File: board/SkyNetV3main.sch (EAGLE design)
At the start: 37 parts, among them IC1 LPC1768, Q1 12MHz, Q2 32.768KHz, U1 HC_05

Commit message: further schematics development; layout started
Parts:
- removed RADIO: RF4463PRO, RF4436PRO:RF4463PRO
- removed U$2: BCX17, skynet_other:BCX17
- removed U$3: UCC3954, UCC3954:UCC3954
- removed U1: HC_05, Bluetooth HC-05:HC_05
- removed USB2: MOLEX-47346-0001, usb_con-update:MOLEX-47346-0001
- added C10: 4u7, rcl:C-EUC1206K
- added C11: 100n, rcl:C-EUC1206K
- added C12, C13, C14, C18, C19, C20, C21: 100n, rcl:C-EUC0603
- added C22, C23: 18p, rcl:C-EUC0603
- added C6: 10u, rcl:C-EUC1206K
- added IC2: RF4463PRO, RF4436PRO:RF4463PRO
- added IC3: LPC1768, lpc1xxx-v6:LPC1768
- added IC4: BCX17, skynet_other:BCX17
- added IC5: TPS63001, texas:TPS6300
- added IC6: MCP73871-2CCI/ML, microchip-battery:MCP73871-2CCI/ML
- added JP3: JTAG, microbuilder:HEADER-2X51.27MM
- added JP4: PERIPH, microbuilder:HEADER-2X51.27MM
- added L1: 2u2, skynet_other:LPS4012
- added OK1, OK2, OK3: PC3H7, skynet_other:PC3H7
- added Q3: IRLM6402, microbuilder:MOSFET-PWIDE
- added Q4: BSS138, microbuilder:MOSFET-NWIDE
- added R11, R12: 10k, rcl:R-EU_R0603
- added R15, R16: 33, rcl:R-EU_R0603
- added R17: 100, rcl:R-EU_R0603
- added R18, R19: 68, rcl:R-EU_R0603
- added S3: INPUT, skynet_other:PT645VERT
- added USB1: MOLEX-47346-0001, usb_con-update:MOLEX-47346-0001
- added X1: BAT, con-molex:22-23-2021
- C1: device capacitor-wima:C2.5/2 -> rcl:C-EUC1206K
- C15: value 100u -> 100n; device rcl:CPOL-EU153CLV-1010 -> rcl:C-EUC0603
- C16, C17: value 18p -> 100n; device capacitor-wima:C2.5/2 -> rcl:C-EUC0603
- C2, C3: value 5p -> 18p; device capacitor-wima:C2.5/2 -> rcl:C-EUC0603
- C4, C5: value 18p -> 33p; device capacitor-wima:C2.5/2 -> rcl:C-EUC0603
- C7, C8: device rcl:C-EUC1206 -> rcl:C-EUC1206K
- C9: value 10u -> 4u7; device rcl:C-EUC1206 -> rcl:C-EUC1206K
- IC1: value LPC1768 -> HC_05; device lpc1xxx-v6:LPC1768 -> Bluetooth HC-05:HC_05
- JP1: value PROG -> MEASURE
- JP2: value ANT -> DEBUG; device pinhead:PINHD-1X2 -> pinhead:PINHD-1X5
- LED1: value OVSTRGBBCR8 -> STATUS; device led:OVSTRGBBCR8 -> skynet_other:RGB-LED
- Q1: value 12MHz -> 32.768KHz; device special:XTAL -> crystal-2:CRYSTALMM20SS
- Q2: value 32.768KHz -> 12MHz; device special:XTAL -> microbuilder:CRYSTALSMD
- R1: value 38,3 -> 10k; device resistor:R-EU_R1206 -> rcl:R-EU_R0603
- R10: value 1k5 -> 560; device resistor:R-EU_R1206 -> rcl:R-EU_R0603
- R13: value 33 -> 10k; device resistor:R-EU_R1206 -> rcl:R-EU_R0603
- R14: value 33 -> 100k; device resistor:R-EU_R1206 -> rcl:R-EU_R0603
- R2: value 24,9 -> 10K; device resistor:R-EU_R1206 -> rcl:R-EU_R0603
- R3: value 38,3 -> 50; device resistor:R-EU_R1206 -> rcl:R-EU_R0603
- R4: value 10K -> 1k5; device resistor:R-EU_R1206 -> rcl:R-EU_R0603
- R5: device resistor:R-EU_R1206 -> rcl:R-EU_R0603
- R6, R8: value 10k -> 91; device rcl:R-EU_R1206 -> rcl:R-EU_R0603
- R7: value 1k -> 91; device rcl:R-EU_R1206 -> rcl:R-EU_R0603
- R9: value 50 -> 10k; device resistor:R-EU_R1206 -> rcl:R-EU_R0603
- S1: value INPUT -> PROG; device switch-omron:10-XX -> switch-ck:PTS645SSMTR
- S2: device switch-omron:10-XX -> switch-ck:PTS645SSMTR
- U$1: value MCP73871-1AAI/ML -> ANT-MML; device microchip-battery:MCP73871-1AAI/ML -> skynet_other:ANT-MML
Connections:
- removed net N$1: IC1.P0[21]/RI1/RD1, RADIO.SDN
- removed net N$10: IC1.P0[0]/RD1/TXD3/SDA1, U1.RX
- removed net N$11: IC1.P0[16]/RXD1/SSEL0/SSEL, RADIO.NSEL
- removed net N$12: IC1.P0[20]/DTR1/SCL1, RADIO.GPIO0
- removed net N$13: IC1.P2[2]/PWM1[3]/CTS1/TRACEDATA[3], R1.1
- removed net N$14: LED1-G.A, R3.2
- removed net N$15: IC1.P2[9]/USB_CONNECT/RXD2/ENET_MDIO, R9.1
- removed net N$16: IC1.P0[18]/DCD1/MOSI0/MOSI, RADIO.SDI
- removed net N$17: IC1.P0[17]/CTS1/MISO0/MISO, RADIO.SDO
- removed net N$18: IC1.P0[15]/TXD1/SCK0/SCK, RADIO.SCLK
- removed net N$2: IC1.P2[10]/EINT0/NMI, JP1.1, R5.1
- removed net N$20: IC1.P0[19]/DSR1/SDA1, RADIO.NIRQ
- removed net N$21: JP2.1, RADIO.ANT
- removed net N$22: R9.2, U$2.B
- removed net N$23: LED1-R.A, R2.2
- removed net N$24: R8.1, U$1.PROG3
- removed net N$25: R7.1, U$1.PROG1
- removed net N$26: R6.1, U$1.THERM
- removed net N$27: LED1G$1.A, R1.2
- removed net N$28: IC1.P2[12]/EINT2/I2STX_WS, S1.P, S1.P1
- removed net N$3: IC1.P2[0]/PWM1[1]/TXD1, R2.1
- removed net N$4: IC1.P2[1]/PWM1[2]/RXD1, R3.1
- removed net N$40: R10.2, U$2.C
- removed net N$44: C15.-, U$3.BAT-
- removed net N$49: R13.2, USB2.2
- removed net N$50: R14.2, USB2.3
- removed net N$9: IC1.P0[1]/TD1/RXD3/SCL1, U1.TX
- new net AD-IN: C15.1, IC3.P0[23]/AD0[0]/I2SRX_CLK/CAP3[0], R12.2, R13.1
- new net AD-PWR: IC3.P0[22]/RTS1/TD1, Q4.G
- new net AD-PWR-FET: Q3.G, Q4.D, R14.2
- new net AD-PWR-FET2: Q3.D, R12.1
- new net ANT: IC2.ANT, U$1.ANT
- new net BT_RX: IC1.RX, IC3.P0[0]/RD1/TXD3/SDA1
- new net BT_TX: IC1.TX, IC3.P0[1]/TD1/RXD3/SCL1
- new net CHGSEL_H: IC3.P1[0]/ENET_TXD0, IC6.SEL
- new net CHGSEL_L: IC3.P1[1]/ENET_TXD1, IC6.PROG2
- new net CHG_S1: IC3.P1[4]/ENET_TX_EN, OK3.COL
- new net CHG_S2: IC3.P1[8]/ENET_CRS, OK2.COL
- new net EXT_GPIO0: IC3.P2[3]/PWM1[4]/DCD1/TRACEDATA[2], JP4.6
- new net EXT_GPIO1: IC3.P2[4]/PWM1[5]/DSR1/TRACEDATA[1], JP4.8
- new net EXT_PWR: IC3.P2[12]/EINT2/I2STX_WS, OK1.COL
- new net INPUT: IC3.P2[11]/EINT1/I2STX_CLK, S3.P
- new net JTAG-TRST: IC3.TRST, R1.1
- new net JTAG_TCK: IC3.TCK/SWDCLK, JP3.4
- new net JTAG_TDI: IC3.TDI, JP3.8
- new net JTAG_TDO: IC3.TDO/SWO, JP3.6
- new net JTAG_TMS: IC3.TMS/SWDIO, JP3.2
- new net L1: IC5G$1.L1, L1.P1
- new net L2: IC5G$1.L2, L1.P2
- new net LED-B-R: LED1-B.A, R19.1
- new net LED-G-R: LED1-G.A, R18.1
- new net LED-R-R: LED1-R.A, R17.1
- new net LED_B: IC3.P2[2]/PWM1[3]/CTS1/TRACEDATA[3], LED1-B.C
- new net LED_G: IC3.P2[1]/PWM1[2]/RXD1, LED1-G.C
- new net LED_R: IC3.P2[0]/PWM1[1]/TXD1, LED1-R.C
- new net OUT2: C10.1, IC6.OUT, IC6.OUT2, JP1.1
- new net PG: IC6./PG, R6.1
- new net PG-OK: OK1.C, R6.2
- new net PROG: IC3.P2[10]/EINT0/NMI, R5.1, S1.P
- new net PROG1: IC6.PROG1, R10.1
- new net PROG3: IC6.PROG3, R9.1
- new net RF-GPIO0: IC2.GPIO0, IC3.P0[20]/DTR1/SCL1
- new net RX: IC3.P0[3]/RXD0/AD0[6], JP2.1
- new net SCL_EXT: IC3.P0[11]/RXD2/SCL2/MAT3[1], JP4.4
- new net SDA_EXT: IC3.P0[10]/TXD2/SDA2/MAT3[0], JP4.2
- new net SDI: IC2.SDI, IC3.P0[18]/DCD1/MOSI0/MOSI
- new net SPI0-NIRQ: IC2.NIRQ, IC3.P0[19]/DSR1/SDA1
- new net SPI0-NSEL: IC2.NSEL, IC3.P0[16]/RXD1/SSEL0/SSEL
- new net SPI0-SCLK: IC2.SCLK, IC3.P0[15]/TXD1/SCK0/SCK
- new net SPI0-SDN: IC2.SDN, IC3.P0[21]/RI1/RD1
- new net SPI0-SDO: IC2.SDO, IC3.P0[17]/CTS1/MISO0/MISO
- new net SPI2_MISO: IC3.P0[8]/I2STX_WS/MISO1/MAT2[2], JP4.5
- new net SPI2_MOSI: IC3.P0[9]/I2STX_SDA/MOSI1/MAT2[3], JP4.7
- new net SPI2_SCK: IC3.P0[7]/I2STX_CLK/SCK1/MAT2[1], JP4.3
- new net SPI2_SEL: IC3.P0[6]/I2SRX_SDA/SSEL1/MAT2[0], JP4.1
- new net STAT1: IC6.STAT1/LBO, R8.1
- new net STAT1-OK: OK3.C, R8.2
- new net STAT2: IC6.STAT2, R7.1
- new net STAT2-OK: OK2.C, R7.2
- new net THERM: IC6.THERM, R11.1
- new net TX: IC3.P0[2]/TXD0/AD0[7], JP2.3
- new net USB-CON: IC3.P2[9]/USB_CONNECT/RXD2/ENET_MDIO, R3.1
- new net USB-CON-TRANS: IC4.B, R3.2
- new net USB-CON-TRANS-2: IC4.C, R4.2
- new net USB-D+_IN: R15.2, USB1.2
- new net USB-D-_IN: R16.2, USB1.3
- net +3V3: now also C11.1, C12.1, C13.1, C14.1, C16.1, C17.1, C18.1, C19.1, C20.1, C21.1, C8.1, IC1.3V3, IC2.VCC, IC3.VBAT, IC3.VDD(3V3)1, IC3.VDD(3V3)2, IC3.VDD(3V3)3, IC3.VDD(3V3)4, IC3.VDD(REG)(3V3)1, IC3.VDD(REG)(3V3)2, IC3.VDDA, IC3.VREFP, IC4.E, IC5G$1.FB, IC5G$1.VOUT, JP2.4, JP3.1, JP4.10, R1.2, R17.2, R18.2, R19.2, R2.2; no longer R4.2, RADIO.VCC, U$2.E, U1.3V3
- net +5V: now also C6.1, IC6./TE, IC6.CE, IC6.IN, IC6.IN2, IC6.VPCC, OK1.A, OK2.A, OK3.A, USB1.1; no longer C7.1, U$1./TE, U$1.CE, U$1.IN, U$1.IN2, U$1.PROG2, U$1.SEL, U$1.VPCC, USB2.1
- net BT_AT: now also IC1.PIO11, IC3.P0[4]/I2SRX_CLK/RD2/CAP2[0]; no longer IC1.P0[4]/I2SRX_CLK/RD2/CAP2[0], U1.PIO11
- net BT_RESET: now also IC1.RST, IC3.P0[5]/I2SRX_WS/TD2/CAP2[1]; no longer IC1.P0[5]/I2SRX_WS/TD2/CAP2[1], U1.RST
- net GND: now also C10.2, C11.2, C12.2, C13.2, C14.2, C15.2, C18.2, C19.2, C20.2, C21.2, C22.2, C23.2, C6.2, IC1.GND, IC2.GND@1, IC2.GND@2, IC2.GND@3, IC3.VREFN, IC3.VSS1, IC3.VSS2, IC3.VSS3, IC3.VSS4, IC3.VSS5, IC3.VSS6, IC3.VSSA, IC5G$1.GND, IC5G$1.PGND, IC6.EP, IC6.VSS, IC6.VSS2, JP2.5, JP3.3, JP3.5, JP3.9, JP4.9, OK1.EMI, OK2.EMI, OK3.EMI, Q4.S, R10.2, R11.2, R13.2, R9.2, S2.P, S3.S, U$1.GND, USB1.5, USB1.GND1, USB1.GND2, USB1.GND3, USB1.GND4, X1-1.S; no longer C15.+, IC1.VREFN, IC1.VSS1, IC1.VSS2, IC1.VSS3, IC1.VSS4, IC1.VSS5, IC1.VSS6, IC1.VSSA, JP1.2, JP2.2, LED1-G.C, LED1-R.C, LED1G$1.C, R6.2, R7.2, R8.2, RADIO.GND$1, RADIO.GND$2, RADIO.GND$3, S1.S1, S2.S, S2.S1, U$1.EP, U$1.VSS, U$1.VSS2, U1.GND, USB2.5
- net RESET: now also IC3.RESET, JP3.10, R2.1, S2.S; no longer IC1.RESET, R4.1, S2.P, S2.P1
- net RTCX1: now also IC3.RTCX1, Q1.2; no longer IC1.RTCX1, Q2.2
- net RTCX2: now also IC3.RTCX2, Q1.1; no longer IC1.RTCX2, Q2.1
- net USB-D+: now also C22.1, IC3.P0[29]/USB_DPLUS, R15.1, R4.1; no longer C16.1, IC1.P0[29]/USB_DPLUS, R10.1, R13.1
- net USB-D-: now also C23.1, IC3.P0[30]/USB_DMINUS, R16.1; no longer C17.1, IC1.P0[30]/USB_DMINUS, R14.1
- net V+: now also C9.1, IC6.VBAT, IC6.VBAT2, IC6.VBAT_SENSE, Q3.S, R14.1, X1-2.S; no longer C8.1, U$1.VBAT, U$1.VBAT2, U$1.VBAT_SENSE
- net VCC: now also C7.1, IC5G$1.EN, IC5G$1.PS/SYNC, IC5G$1.VIN, IC5G$1.VINA, JP1.2; no longer C9.1, IC1.VBAT, IC1.VDD(3V3)1, IC1.VDD(3V3)2, IC1.VDD(3V3)3, IC1.VDD(3V3)4, IC1.VDD(REG)(3V3)1, IC1.VDD(REG)(3V3)2, IC1.VDDA, IC1.VREFP, U$1.OUT, U$1.OUT2
- net XTAL1: now also IC3.XTAL1, Q2.2; no longer IC1.XTAL1, Q1.2
- net XTAL2: now also IC3.XTAL2, Q2.1; no longer IC1.XTAL2, Q1.1
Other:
- note removed: "TODO: ISP-Header"
- note removed: "TODO: wie erkennen ob USB-Flashen?"

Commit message: further layout, got stuck somewhere...
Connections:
- removed net BT_RESET: IC1.RST, IC3.P0[5]/I2SRX_WS/TD2/CAP2[1]
- new net BT-RST: IC1.RST, IC3.P0[22]/RTS1/TD1
- net AD-PWR: now also IC3.P1[29]/MCOB2/PCAP1[1]/MAT0[1]; no longer IC3.P0[22]/RTS1/TD1
- net BT_AT: now also IC3.P2[5]/PWM1[6]/DTR1/TRACEDATA[0]; no longer IC3.P0[4]/I2SRX_CLK/RD2/CAP2[0]
- net CHGSEL_H: now also IC3.P3[25]/MAT0[0]/PWM1[2]; no longer IC3.P1[0]/ENET_TXD0
- net CHGSEL_L: now also IC3.P3[26]/STCLK/MAT0[1]/PWM1[3]; no longer IC3.P1[1]/ENET_TXD1
- net CHG_S1: now also IC3.P0[10]/TXD2/SDA2/MAT3[0]; no longer IC3.P1[4]/ENET_TX_EN
- net CHG_S2: now also IC3.P0[11]/RXD2/SCL2/MAT3[1]; no longer IC3.P1[8]/ENET_CRS
- net SCL_EXT: now also IC3.P0[28]/SCL0/USB_SCL; no longer IC3.P0[11]/RXD2/SCL2/MAT3[1]
- net SDA_EXT: now also IC3.P0[27]/SDA0/USB_SDA; no longer IC3.P0[10]/TXD2/SDA2/MAT3[0]
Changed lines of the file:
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@@
 <net name="BT_AT" class="0">
+<segment>
+<pinref part="IC3" gate="G$1" pin="P2[5]/PWM1[6]/DTR1/TRACEDATA[0]"/>
+<wire x1="185.42" y1="88.9" x2="187.96" y2="88.9" width="0.1524" layer="91"/>
+<label x="188.214" y="87.884" size="1.778" layer="95"/>
+</segment>
 <segment>
 <pinref part="IC1" gate="G$1" pin="PIO11"/>
 <wire x1="10.16" y1="162.56" x2="7.62" y2="162.56" width="0.1524" layer="91"/>
-<wire x1="7.62" y1="162.56" x2="7.62" y2="172.72" width="0.1524" layer="91"/>
-<wire x1="7.62" y1="172.72" x2="73.66" y2="172.72" width="0.1524" layer="91"/>
-<wire x1="73.66" y1="172.72" x2="73.66" y2="154.94" width="0.1524" layer="91"/>
-<pinref part="IC3" gate="G$1" pin="P0[4]/I2SRX_CLK/RD2/CAP2[0]"/>
-<wire x1="73.66" y1="154.94" x2="96.52" y2="154.94" width="0.1524" layer="91"/>
+<label x="4.572" y="168.402" size="1.778" layer="95"/>
+<wire x1="7.62" y1="162.56" x2="7.62" y2="167.64" width="0.1524" layer="91"/>
 </segment>
 </net>
@@
 </segment>
 </net>
-<net name="BT_RESET" class="0">
-<segment>
-<pinref part="IC1" gate="G$1" pin="RST"/>
-<wire x1="58.42" y1="137.16" x2="60.96" y2="137.16" width="0.1524" layer="91"/>
-<wire x1="60.96" y1="137.16" x2="60.96" y2="152.4" width="0.1524" layer="91"/>
-<pinref part="IC3" gate="G$1" pin="P0[5]/I2SRX_WS/TD2/CAP2[1]"/>
-<wire x1="60.96" y1="152.4" x2="96.52" y2="152.4" width="0.1524" layer="91"/>
-</segment>
-</net>
 <net name="RF-GPIO0" class="0">
 <segment>
@@
 <net name="CHGSEL_H" class="0">
 <segment>
-<pinref part="IC3" gate="G$1" pin="P1[0]/ENET_TXD0"/>
-<wire x1="185.42" y1="165.1" x2="193.04" y2="165.1" width="0.1524" layer="91"/>
-<label x="193.802" y="164.338" size="1.778" layer="95"/>
+<pinref part="IC3" gate="G$1" pin="P3[25]/MAT0[0]/PWM1[2]"/>
+<wire x1="185.42" y1="63.5" x2="187.96" y2="63.5" width="0.1524" layer="91"/>
+<wire x1="187.96" y1="63.5" x2="187.96" y2="68.58" width="0.1524" layer="91"/>
+<wire x1="187.96" y1="68.58" x2="193.04" y2="68.58" width="0.1524" layer="91"/>
+<label x="193.294" y="67.564" size="1.778" layer="95"/>
 </segment>
 </net>
 <net name="CHGSEL_L" class="0">
 <segment>
-<pinref part="IC3" gate="G$1" pin="P1[1]/ENET_TXD1"/>
-<wire x1="185.42" y1="162.56" x2="193.04" y2="162.56" width="0.1524" layer="91"/>
-<label x="193.802" y="161.798" size="1.778" layer="95"/>
+<pinref part="IC3" gate="G$1" pin="P3[26]/STCLK/MAT0[1]/PWM1[3]"/>
+<wire x1="185.42" y1="60.96" x2="190.5" y2="60.96" width="0.1524" layer="91"/>
+<wire x1="190.5" y1="60.96" x2="190.5" y2="66.04" width="0.1524" layer="91"/>
+<wire x1="190.5" y1="66.04" x2="193.04" y2="66.04" width="0.1524" layer="91"/>
+<label x="193.294" y="65.024" size="1.778" layer="95"/>
 </segment>
 </net>
@@
 <net name="CHG_S1" class="0">
 <segment>
-<pinref part="IC3" gate="G$1" pin="P1[4]/ENET_TX_EN"/>
-<wire x1="185.42" y1="160.02" x2="193.04" y2="160.02" width="0.1524" layer="91"/>
-<label x="193.802" y="159.258" size="1.778" layer="95"/>
+<pinref part="IC3" gate="G$1" pin="P0[10]/TXD2/SDA2/MAT3[0]"/>
+<wire x1="96.52" y1="139.7" x2="93.98" y2="139.7" width="0.1524" layer="91"/>
+<label x="92.964" y="139.192" size="1.778" layer="95" rot="MR0"/>
 </segment>
 </net>
 <net name="CHG_S2" class="0">
 <segment>
-<pinref part="IC3" gate="G$1" pin="P1[8]/ENET_CRS"/>
-<wire x1="185.42" y1="157.48" x2="193.04" y2="157.48" width="0.1524" layer="91"/>
-<label x="193.802" y="156.718" size="1.778" layer="95"/>
+<pinref part="IC3" gate="G$1" pin="P0[11]/RXD2/SCL2/MAT3[1]"/>
+<wire x1="96.52" y1="137.16" x2="93.98" y2="137.16" width="0.1524" layer="91"/>
+<label x="92.964" y="136.652" size="1.778" layer="95" rot="MR0"/>
 </segment>
 </net>
@@
 <net name="SDA_EXT" class="0">
 <segment>
-<pinref part="IC3" gate="G$1" pin="P0[10]/TXD2/SDA2/MAT3[0]"/>
-<wire x1="96.52" y1="139.7" x2="93.98" y2="139.7" width="0.1524" layer="91"/>
-<label x="92.964" y="139.192" size="1.778" layer="95" rot="MR0"/>
+<pinref part="IC3" gate="G$1" pin="P0[27]/SDA0/USB_SDA"/>
+<wire x1="96.52" y1="104.14" x2="93.98" y2="104.14" width="0.1524" layer="91"/>
+<label x="93.472" y="103.378" size="1.778" layer="95" rot="MR0"/>
 </segment>
 </net>
 <net name="SCL_EXT" class="0">
 <segment>
-<pinref part="IC3" gate="G$1" pin="P0[11]/RXD2/SCL2/MAT3[1]"/>
-<wire x1="96.52" y1="137.16" x2="93.98" y2="137.16" width="0.1524" layer="91"/>
-<label x="92.964" y="136.652" size="1.778" layer="95" rot="MR0"/>
+<pinref part="IC3" gate="G$1" pin="P0[28]/SCL0/USB_SCL"/>
+<wire x1="96.52" y1="101.6" x2="93.98" y2="101.6" width="0.1524" layer="91"/>
+<label x="93.472" y="100.838" size="1.778" layer="95" rot="MR0"/>
 </segment>
 </net>
 <net name="AD-PWR" class="0">
+<segment>
+<pinref part="IC3" gate="G$1" pin="P1[29]/MCOB2/PCAP1[1]/MAT0[1]"/>
+<wire x1="185.42" y1="111.76" x2="187.96" y2="111.76" width="0.1524" layer="91"/>
+<label x="188.214" y="110.998" size="1.778" layer="95"/>
+</segment>
+</net>
+<net name="JTAG-TRST" class="0">
+<segment>
+<pinref part="R1" gate="G$1" pin="1"/>
+<pinref part="IC3" gate="G$1" pin="TRST"/>
+<wire x1="71.12" y1="20.32" x2="96.52" y2="20.32" width="0.1524" layer="91"/>
+</segment>
+</net>
+<net name="LED_R" class="0">
+<segment>
+<pinref part="IC3" gate="G$1" pin="P2[0]/PWM1[1]/TXD1"/>
+<wire x1="185.42" y1="101.6" x2="187.96" y2="101.6" width="0.1524" layer="91"/>
+<label x="188.214" y="100.838" size="1.778" layer="95"/>
+</segment>
+</net>
+<net name="LED_B" class="0">
+<segment>
+<pinref part="IC3" gate="G$1" pin="P2[2]/PWM1[3]/CTS1/TRACEDATA[3]"/>
+<wire x1="185.42" y1="96.52" x2="187.96" y2="96.52" width="0.1524" layer="91"/>
+<label x="188.214" y="95.758" size="1.778" layer="95"/>
+</segment>
+</net>
+<net name="BT-RST" class="0">
 <segment>
 <pinref part="IC3" gate="G$1" pin="P0[22]/RTS1/TD1"/>
@@
 <label x="93.472" y="116.078" size="1.778" layer="95" rot="MR0"/>
 </segment>
-</net>
-<net name="JTAG-TRST" class="0">
-<segment>
-<pinref part="R1" gate="G$1" pin="1"/>
-<pinref part="IC3" gate="G$1" pin="TRST"/>
-<wire x1="71.12" y1="20.32" x2="96.52" y2="20.32" width="0.1524" layer="91"/>
-</segment>
-</net>
-<net name="LED_R" class="0">
-<segment>
-<pinref part="IC3" gate="G$1" pin="P2[0]/PWM1[1]/TXD1"/>
-<wire x1="185.42" y1="101.6" x2="187.96" y2="101.6" width="0.1524" layer="91"/>
-<label x="188.214" y="100.838" size="1.778" layer="95"/>
-</segment>
-</net>
-<net name="LED_B" class="0">
-<segment>
-<pinref part="IC3" gate="G$1" pin="P2[2]/PWM1[3]/CTS1/TRACEDATA[3]"/>
-<wire x1="185.42" y1="96.52" x2="187.96" y2="96.52" width="0.1524" layer="91"/>
-<label x="188.214" y="95.758" size="1.778" layer="95"/>
-</segment>
-</net>
+<segment>
+<pinref part="IC1" gate="G$1" pin="RST"/>
+<wire x1="58.42" y1="137.16" x2="60.96" y2="137.16" width="0.1524" layer="91"/>
+<wire x1="60.96" y1="137.16" x2="60.96" y2="142.24" width="0.1524" layer="91"/>
+<label x="59.69" y="142.494" size="1.778" layer="95"/>
+</segment>
+</net>

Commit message: added ground planes
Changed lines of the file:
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@@
 <pinref part="GND26" gate="1" pin="GND"/>
 <wire x1="88.9" y1="38.1" x2="88.9" y2="40.64" width="0.1524" layer="91"/>
-<pinref part="IC3" gate="G$1" pin="VSS6"/>
-<wire x1="96.52" y1="33.02" x2="93.98" y2="33.02" width="0.1524" layer="91"/>
-<wire x1="93.98" y1="33.02" x2="93.98" y2="35.56" width="0.1524" layer="91"/>
 <pinref part="IC3" gate="G$1" pin="VSS1"/>
-<wire x1="93.98" y1="35.56" x2="93.98" y2="38.1" width="0.1524" layer="91"/>
 <wire x1="93.98" y1="38.1" x2="93.98" y2="40.64" width="0.1524" layer="91"/>
 <wire x1="93.98" y1="40.64" x2="93.98" y2="43.18" width="0.1524" layer="91"/>
@@
 <pinref part="IC3" gate="G$1" pin="VSS4"/>
 <wire x1="96.52" y1="38.1" x2="93.98" y2="38.1" width="0.1524" layer="91"/>
-<junction x="93.98" y="38.1"/>
-<pinref part="IC3" gate="G$1" pin="VSS5"/>
-<wire x1="96.52" y1="35.56" x2="93.98" y2="35.56" width="0.1524" layer="91"/>
-<junction x="93.98" y="35.56"/>
 <wire x1="88.9" y1="40.64" x2="93.98" y2="40.64" width="0.1524" layer="91"/>
 <wire x1="93.98" y1="45.72" x2="93.98" y2="50.8" width="0.1524" layer="91"/>
@@
 <wire x1="93.98" y1="58.42" x2="93.98" y2="50.8" width="0.1524" layer="91"/>
 <junction x="93.98" y="50.8"/>
+<pinref part="IC3" gate="G$1" pin="VSS5"/>
+<wire x1="93.98" y1="38.1" x2="93.98" y2="35.56" width="0.1524" layer="91"/>
+<wire x1="93.98" y1="35.56" x2="96.52" y2="35.56" width="0.1524" layer="91"/>
+<junction x="93.98" y="38.1"/>
+<pinref part="IC3" gate="G$1" pin="VSS6"/>
+<wire x1="93.98" y1="35.56" x2="93.98" y2="33.02" width="0.1524" layer="91"/>
+<wire x1="93.98" y1="33.02" x2="96.52" y2="33.02" width="0.1524" layer="91"/>
+<junction x="93.98" y="35.56"/>
 </segment>
 <segment>

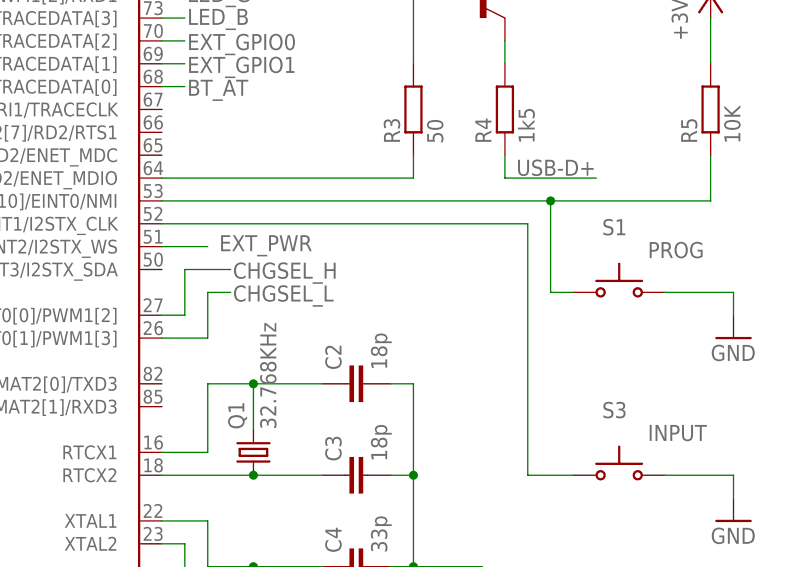
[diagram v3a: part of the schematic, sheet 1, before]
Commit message: layout optimizations, tStop corrected
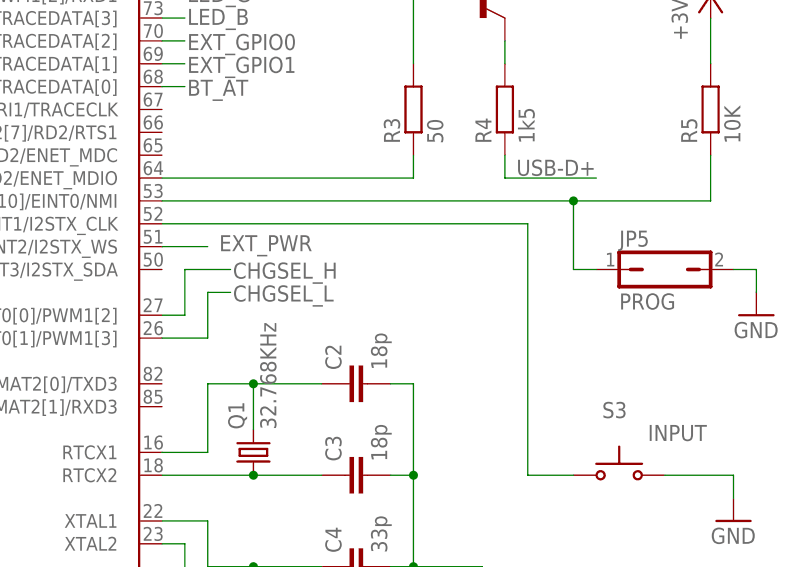
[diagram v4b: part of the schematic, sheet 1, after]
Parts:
- removed S1: PROG, switch-ck:PTS645SSMTR
- added JP5: PROG, jumper:JP1Q
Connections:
- net GND: now also JP5.2; no longer S1.S
- net PROG: now also JP5.1; no longer S1.P
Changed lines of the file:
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@@
 <part name="+3V11" library="supply1" deviceset="+3V3" device=""/>
 <part name="GND13" library="supply1" deviceset="GND" device=""/>
-<part name="S1" library="switch-ck" deviceset="PTS645S???SMTR" device="" value="PROG"/>
 <part name="JP3" library="microbuilder" deviceset="HEADER-2X5" device="1.27MM" value="JTAG"/>
 <part name="+3V12" library="supply1" deviceset="+3V3" device=""/>
@@
 <part name="GND21" library="supply1" deviceset="GND" device=""/>
 <part name="+3V22" library="supply1" deviceset="+3V3" device=""/>
+<part name="JP5" library="jumper" deviceset="JP1Q" device="" value="PROG"/>
 </parts>
 <sheets>
@@
 <instance part="R2" gate="G$1" x="68.58" y="66.04" rot="MR0"/>
 <instance part="+3V2" gate="G$1" x="58.42" y="73.66" rot="MR0"/>
-<instance part="GND5" gate="1" x="248.92" y="60.96"/>
+<instance part="GND5" gate="1" x="251.46" y="63.5"/>
 <instance part="GND6" gate="1" x="248.92" y="40.64"/>
 <instance part="GND7" gate="1" x="220.98" y="27.94"/>
@@
 <instance part="S3" gate="G$1" x="236.22" y="45.72"/>
 <instance part="C1" gate="G$1" x="12.7" y="109.22" rot="MR0"/>
-<instance part="S1" gate="G$1" x="236.22" y="66.04" rot="R270"/>
+<instance part="JP5" gate="A" x="241.3" y="68.58" rot="R270"/>
 </instances>
 <busses>
@@
 </segment>
 <segment>
-<pinref part="GND5" gate="1" pin="GND"/>
-<wire x1="248.92" y1="63.5" x2="248.92" y2="66.04" width="0.1524" layer="91"/>
-<pinref part="S1" gate="G$1" pin="S"/>
-<wire x1="241.3" y1="66.04" x2="248.92" y2="66.04" width="0.1524" layer="91"/>
-</segment>
-<segment>
 <pinref part="C5" gate="G$1" pin="2"/>
 <wire x1="210.82" y1="27.94" x2="213.36" y2="27.94" width="0.1524" layer="91"/>
@@
 <wire x1="17.78" y1="101.6" x2="12.7" y2="101.6" width="0.1524" layer="91"/>
 <junction x="12.7" y="101.6"/>
+</segment>
+<segment>
+<pinref part="GND5" gate="1" pin="GND"/>
+<pinref part="JP5" gate="A" pin="2"/>
+<wire x1="251.46" y1="66.04" x2="251.46" y2="68.58" width="0.1524" layer="91"/>
+<wire x1="251.46" y1="68.58" x2="248.92" y2="68.58" width="0.1524" layer="91"/>
 </segment>
 </net>
@@
 <segment>
 <pinref part="IC3" gate="G$1" pin="P2[10]/EINT0/NMI"/>
-<wire x1="185.42" y1="76.2" x2="228.6" y2="76.2" width="0.1524" layer="91"/>
-<wire x1="228.6" y1="76.2" x2="228.6" y2="66.04" width="0.1524" layer="91"/>
+<wire x1="185.42" y1="76.2" x2="231.14" y2="76.2" width="0.1524" layer="91"/>
 <pinref part="R5" gate="G$1" pin="1"/>
-<wire x1="228.6" y1="76.2" x2="246.38" y2="76.2" width="0.1524" layer="91"/>
+<wire x1="231.14" y1="76.2" x2="246.38" y2="76.2" width="0.1524" layer="91"/>
 <wire x1="246.38" y1="76.2" x2="246.38" y2="81.28" width="0.1524" layer="91"/>
-<junction x="228.6" y="76.2"/>
-<pinref part="S1" gate="G$1" pin="P"/>
-<wire x1="228.6" y1="66.04" x2="231.14" y2="66.04" width="0.1524" layer="91"/>
-</segment>
-</net>
+<pinref part="JP5" gate="A" pin="1"/>
+<wire x1="233.68" y1="68.58" x2="231.14" y2="68.58" width="0.1524" layer="91"/>
+<wire x1="231.14" y1="68.58" x2="231.14" y2="76.2" width="0.1524" layer="91"/>
+<junction x="231.14" y="76.2"/>
+</segment>
+</net>
